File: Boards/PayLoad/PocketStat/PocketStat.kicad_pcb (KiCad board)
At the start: 4 copper layers, 46 x 46 mm, 71 parts, among them J20 DX07S016JA1R1500, J3 MEM2061-01-188-00-A_REVA, J5 BM03B-SRSS-TBLFSN, Q1 BC857CMB_315, U1 HDC2080DMBR, U4 LPS22DFTR, U5 W25Q128JVSIQ TR, U6 BMP581, U8 ST1L05APU33R

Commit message: PocketStat update
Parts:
- removed R1, R2: 2k, Resistor-0402:RES_0402
- added R26: 2k, Resistor-0402:RES_0402, F.Cu at (126.6, 96.9)
- added R27: 2k, Resistor-0402:RES_0402, F.Cu at (124.1, 98.3)
- moved C1 12.6 mm to (121.2, 96.1), turned to -90 degrees
- moved C5 11.6 mm to (132.3, 98.5), turned to 0 degrees
- moved C13 11.6 mm to (130.9, 78.2), turned to 180 degrees
- moved C3 10.3 mm to (130.9, 79.5), turned to 0 degrees
- moved C2 9.09 mm to (122.5, 96.1), turned to -90 degrees
- moved CR1 9.05 mm to (141.2, 79.7), turned to 0 degrees
- moved U6 8.37 mm to (130.9, 81.6), turned to 0 degrees
- moved HM1 8.37 mm to (132.3, 96.3)
- moved C4 8.29 mm to (130.1, 96.4)
- moved U4 7.52 mm to (124.5, 96.3), turned to 90 degrees
- moved Q1 6.59 mm to (135.3, 78.9), turned to 90 degrees
- moved R20 6.29 mm to (137.2, 79.2), turned to 180 degrees
- moved C24 5.75 mm to (141.0, 75.2), turned to -90 degrees
- moved R21 4.68 mm to (137.2, 80.4), turned to 180 degrees
- moved C22 3.75 mm to (139.8, 75.2), turned to -90 degrees
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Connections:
- HM1 pad 2: +3.3V -> /HUM ~{CS} SPI
- HM1 pad 3: /SDA1 I2C -> /MOSI1 SPI
- HM1 pad 4: /SCL1 I2C -> /SCK1 SPI
- HM1 pad 5: GND -> /MISO1 SPI
- MCU2 pad 12: /BAR1 ~{CS} SPI -> /HUM ~{CS} SPI
- MCU2 pad 15: /BAR2 RDY -> unconnected-(MCU2-GPIO12-Pad15)
- MCU2 pad 16: /BAR2 ~{CS} SPI -> unconnected-(MCU2-GPIO13-Pad16)
- MCU2 pad 18: unconnected-(MCU2-GPIO15-Pad18) -> /LED Status
- MCU2 pad 2: unconnected-(MCU2-GPIO0-Pad2) -> /BAR1 RDY
- MCU2 pad 31: /LED Status -> unconnected-(MCU2-GPIO20-Pad31)
- MCU2 pad 32: unconnected-(MCU2-GPIO21-Pad32) -> /BAR2 RDY
- MCU2 pad 35: /Humidity RDY -> unconnected-(MCU2-GPIO23-Pad35)
- MCU2 pad 38: unconnected-(MCU2-GPIO26_ADC0-Pad38) -> /Humidity RDY
- MCU2 pad 6: /BAR1 RDY -> unconnected-(MCU2-GPIO4-Pad6)
- U4 pad 2: /SCK1 SPI -> /SCL1 I2C
- U4 pad 4: /MOSI1 SPI -> /SDA1 I2C
- U4 pad 5: /MISO1 SPI -> GND
- U4 pad 6: /BAR1 ~{CS} SPI -> +3.3V
- U6 pad 2: /SCK1 SPI -> /SCL0 I2C
- U6 pad 4: /MOSI1 SPI -> /SDA0 I2C
- U6 pad 5: /MISO1 SPI -> GND
- U6 pad 6: /BAR2 ~{CS} SPI -> unconnected-(U6-CSB-Pad6)
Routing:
- net /LED Status: track 3.05 -> 16.2 mm, vias 0 -> 2
- net /BAR1 ~{CS} SPI: track 6.76 -> 0.00 mm, vias 2 -> 0
- net /SCK1 SPI: track 6.46 -> 0.00 mm, vias 2 -> 0
- net /SCL1 I2C: track 4.58 -> 9.56 mm, vias 0 -> 2
- net +6V: track 0.00 -> 4.17 mm, vias 0 -> 1
- net /Crystal: track 0.00 -> 4.13 mm
- net GND: track 5.94 -> 9.88 mm
- net +3.3V: track 29.2 -> 33.0 mm
- net VBUS: track 11.5 -> 15.2 mm
- net /Humidity RDY: track 0.00 -> 3.49 mm, vias 0 -> 1
- net /MISO1 SPI: track 2.92 -> 0.00 mm
- net /HUM ~{CS} SPI: track 0.00 -> 2.69 mm
- net /MOSI1 SPI: track 2.63 -> 0.00 mm
- net /BAR1 RDY: track 6.12 -> 3.50 mm
- net /D+: track 14.3 -> 13.7 mm
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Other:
- board size 46 x 46 mm -> 45.5 x 45.5 mm

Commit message: Pocket Stat Lib update
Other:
- board text added: "TODO: 1- Fazer BOOM e atualizar excel de componentes 2- Routing crítico (Sinais Digitais) -> Fazer DRC no fim 3- Routing +3.3V -> Fazer DRC no fim 4- Routing +6V -> Fazer DRC no fim 5- Routing GND (Fazer ground planes) -> Fazer DRC no fim 6- Adicionar Test Points (GND, +3V3, +6V) 7- Fazer Silkscreen Bonito (Vai se ter de editar o Silkcreen de algumas footprints) (+ Assinar e Logo da PST) 8- Prepa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"
- board text removed: "TODO: 1- Routing crítico (Sinais Digitais) -> Fazer DRC no fim 2- Routing +3.3V -> Fazer DRC no fim 3- Routing +6V -> Fazer DRC no fim 4- Routing GND (Fazer ground planes) -> Fazer DRC no fim 5- Adicionar Test Points (GND, +3V3, +6V) 7- Fazer Silkscreen Bonito (Vai se ter de editar o Silkcreen de algumas footprints) (+ Assinar e Logo da PST) 8- Fazer BOOM e atualizar excel de componentes 9- Prepa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"
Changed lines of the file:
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@@
 			)
 		)
-		(fp_text user "${REFERENCE}"
-			(at 0 0 90)
+		(fp_text user "*"
+			(at -2.3114 -2.6162 90)
 			(unlocked yes)
 			(layer "F.Fab")
@@
 			)
 		)
-		(fp_text user "*"
-			(at -2.3114 -2.6162 90)
+		(fp_text user "${REFERENCE}"
+			(at 0 0 90)
 			(unlocked yes)
 			(layer "F.Fab")
@@
 		(layer "User.4")
 	)
-	(gr_text "TODO:\n1- Routing crítico (Sinais Digitais) -> Fazer DRC no fim\n2- Routing +3.3V -> Fazer DRC no fim\n3- Routing +6V  -> Fazer DRC no fim\n4- Routing GND (Fazer ground planes) -> Fazer DRC no fim\n5- Adicionar Test Points (GND, +3V3, +6V)\n7- Fazer Silkscreen Bonito\n(Vai se ter de editar o Silkcreen de algumas footprints)\n(+ Assinar e Logo da PST)\n8- Fazer BOOM e atualizar excel de componentes\n9- Preparar ficheiros de fabrico -> Tapeout\n---\nO Stackup é:\nTop Layer: Signal/PWR\nInner Layer 1: GND\nInner Layer 2: GND\nBottom Layer: Signal/PWR"
+	(gr_text "TODO:\n1- Fazer BOOM e atualizar excel de componentes\n2- Routing crítico (Sinais Digitais) -> Fazer DRC no fim\n3- Routing +3.3V -> Fazer DRC no fim\n4- Routing +6V  -> Fazer DRC no fim\n5- Routing GND (Fazer ground planes) -> Fazer DRC no fim\n6- Adicionar Test Points (GND, +3V3, +6V)\n7- Fazer Silkscreen Bonito\n(Vai se ter de editar o Silkcreen de algumas footprints)\n(+ Assinar e Logo da PST)\n8- Preparar ficheiros de fabrico -> Tapeout\n---\nO Stackup é:\nTop Layer: Signal/PWR\nInner Layer 1: GND\nInner Layer 2: GND\nBottom Layer: Signal/PWR"
 		(at 99.4 142.45 0)
 		(layer "User.1")
@@
 		(net 6)
 	)
-	(segment
-		(start 113.221499 94.796501)
-		(end 113.3 94.875002)
-		(width 0.5)
-		(layer "F.Cu")
-		(net 6)
-	)
 	(via
 		(at 114.349999 91.9)
@@
 	)
 	(segment
-		(start 125.2 81.05)
-		(end 125.9 81.75)
+		(start 125.9 81.75)
+		(end 127.2 81.75)
 		(width 0.125)
 		(layer "B.Cu")
@@
 	)
 	(segment
-		(start 125.9 81.75)
-		(end 127.2 81.75)
+		(start 125.2 81.05)
+		(end 125.9 81.75)
 		(width 0.125)
 		(layer "B.Cu")
@@
 	)
 	(segment
-		(start 126.381009 92.578145)
+		(start 126.381009 92.573519)
 		(end 126.381009 92.56231)
 		(width 0.125)
@@
 	)
 	(segment
-		(start 118.685 92.615)
-		(end 119.2 92.1)
-		(width 0.25)
+		(start 126.377296 92.577232)
+		(end 126.381009 92.573519)
+		(width 0.125)
 		(layer "F.Cu")
 		(net 52)
 	)
 	(segment
-		(start 126.381009 92.56231)
-		(end 125.918698 92.099999)
-		(width 0.125)
+		(start 118.685 92.615)
+		(end 119.2 92.1)
+		(width 0.25)
 		(layer "F.Cu")
 		(net 52)
@@
 		(net 52)
 	)
+	(segment
+		(start 126.381009 92.56231)
+		(end 125.918698 92.099999)
+		(width 0.125)
+		(layer "F.Cu")
+		(net 52)
+	)
 	(via
 		(at 119.2 92.1)
@@
 	)
 	(via
-		(at 126.381009 92.578145)
+		(at 126.377296 92.577232)
 		(size 0.5)
 		(drill 0.2)
@@
 	)
 	(segment
-		(start 126.4 91.7)
-		(end 125.2964 91.7)
+		(start 126.546312 91.846312)
+		(end 126.4 91.7)
 		(width 0.125)
 		(layer "F.Cu")
@@
 	)
 	(segment
-		(start 126.546312 91.846312)
-		(end 126.4 91.7)
+		(start 126.4 91.7)
+		(end 125.2964 91.7)
 		(width 0.125)
 		(layer "F.Cu")
@@
 	)
 	(segment
-		(start 126.348372 91.7)
-		(end 120.2 91.7)
+		(start 126.546312 91.89794)
+		(end 126.348372 91.7)
 		(width 0.125)
 		(layer "B.Cu")
@@
 	)
 	(segment
-		(start 126.546312 91.89794)
-		(end 126.348372 91.7)
+		(start 126.348372 91.7)
+		(end 120.2 91.7)
 		(width 0.125)
 		(layer "B.Cu")

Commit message: pocketstat power update
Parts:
- D1, D2: value RSX301L-30DDTE25 -> PMEG2010ER; footprint Diode-Schottky_RSX301L:DIOM5026X220N -> Diode-Schottky_PMEG2010ER:SODFL3517X110N
- moved C27 1.62 mm to (122.6, 57.3)
- moved C6 1.62 mm to (122.6, 56.1)
- moved D1 1.35 mm to (111.6, 93.6)
- moved JP4 1.35 mm to (112.4, 96.7)
- moved R22 0.96 mm to (115.3, 96.6), turned to 0 degrees
- moved D2 0.55 mm to (118.6, 56.6)
- moved JP6 0.46 mm to (113.6, 56.8)
- moved BT1 0.46 mm to (112.6, 71.5)
- moved R10 0.26 mm to (113.7, 90.3)
- moved C36 0.26 mm to (112.6, 91.6)
- moved D4 0.26 mm to (110.7, 89.7)
- moved J20 0.26 mm to (105.7, 90.2)
- moved R11 0.26 mm to (113.7, 89.1)
- moved R24 0.26 mm to (109.2, 91.6)
- moved R9 0.26 mm to (108.5, 87.6)
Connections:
- C22 pad 2: +6V -> +5V
- C24 pad 2: +6V -> +5V
- C27 pad 1: +6V -> +5V
- C36 pad 1: +6V -> +5V
- C6 pad 1: +6V -> +5V
- CR1 pad 2: +6V -> +5V
- JP6 pad 1: Net-(D2-A) -> Net-(JP6-A)
- U8 pad 3: +6V -> +5V
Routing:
- net +5V: track 0.00 -> 5.93 mm, vias 0 -> 1
- net +6V: track 4.06 -> 0.00 mm, vias 1 -> 0
- net Net-(JP6-A): track 0.00 -> 2.88 mm
- net Net-(D2-A): track 2.52 -> 0.00 mm
- removed copper zone on F.Cu, net +6V

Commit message: update
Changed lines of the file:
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@@
 		)
 		(fp_text user "*"
-			(at -1.535 -0.881 0)
+			(at -0.959999 -0.631 0)
 			(unlocked yes)
 			(layer "F.SilkS")
@@
 		)
 		(fp_text user "*"
-			(at -1.535 -0.881 0)
+			(at -0.969999 -0.633001 0)
 			(unlocked yes)
 			(layer "F.SilkS")

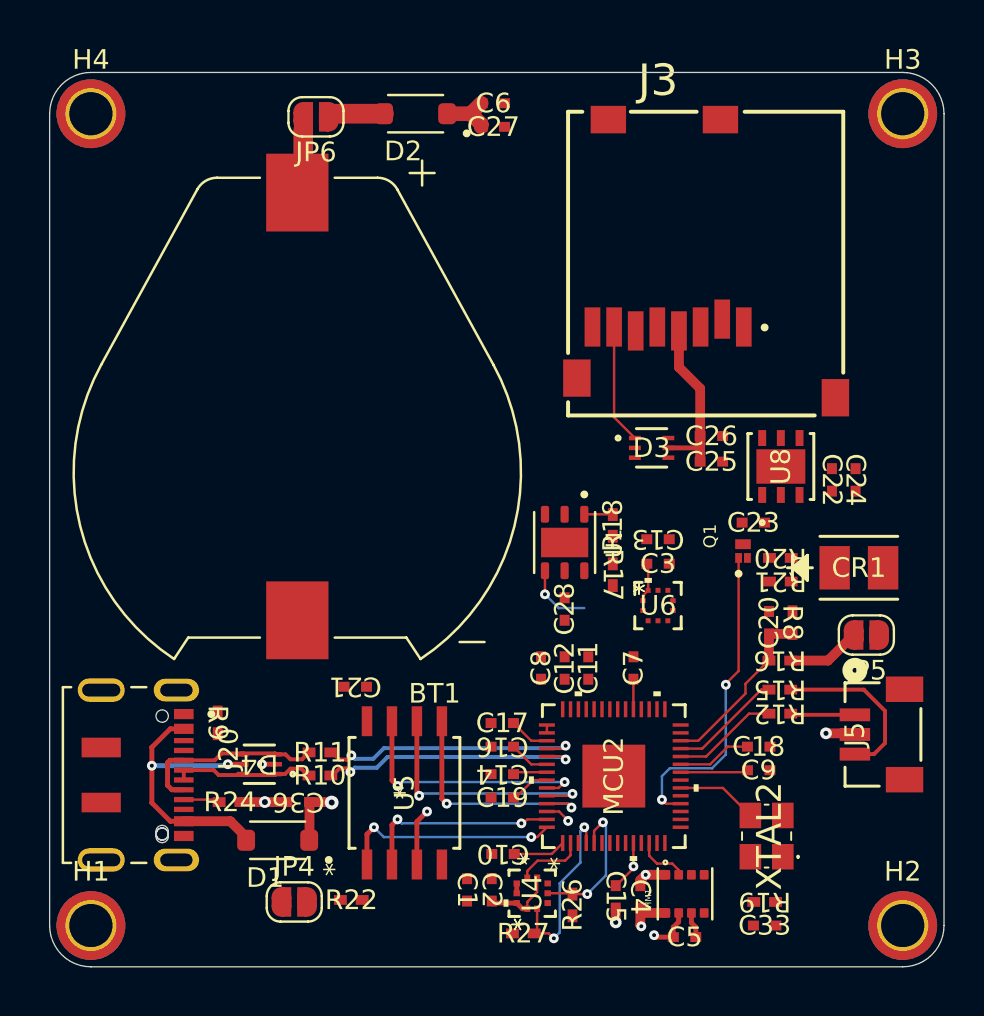
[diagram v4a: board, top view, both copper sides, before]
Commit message: Update PCB Payload
Acabei o routing do ground e coloquei as camadas de GND;
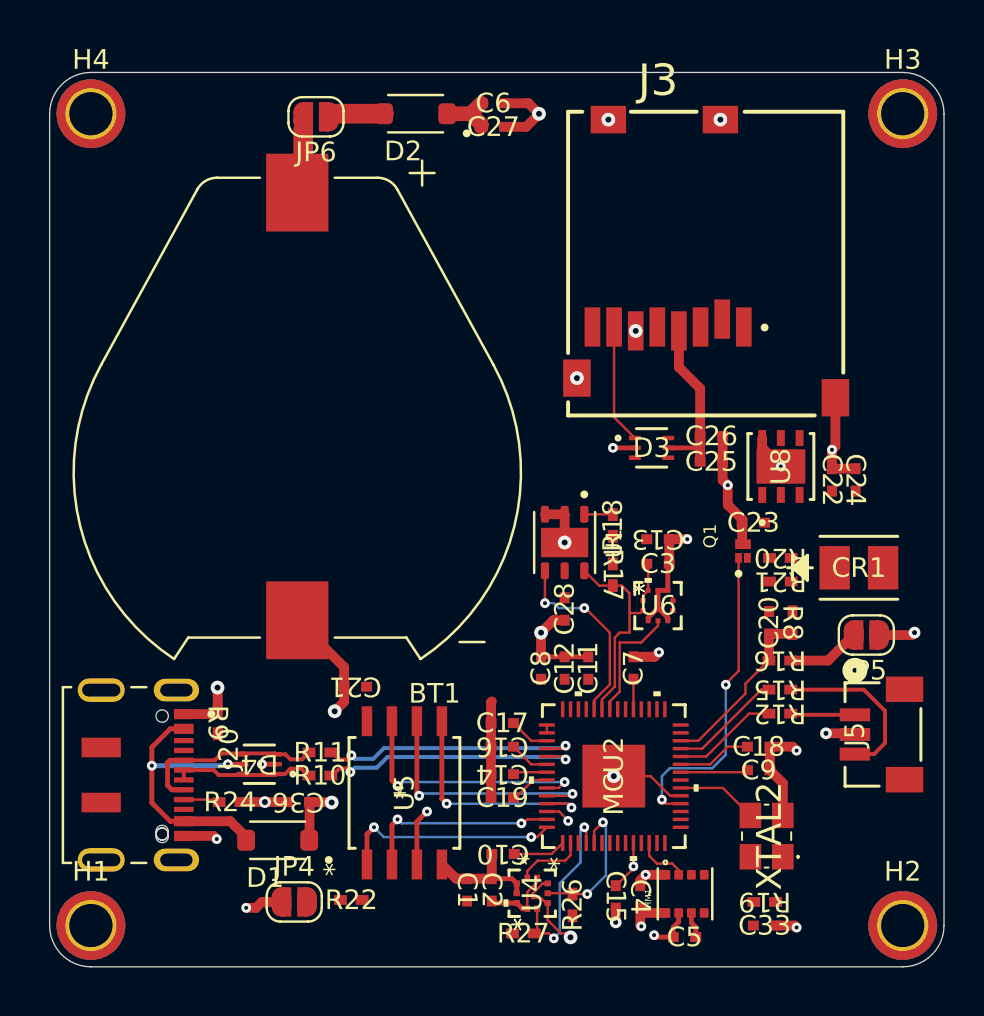
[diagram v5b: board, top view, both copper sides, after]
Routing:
- net GND: track 9.88 -> 82.6 mm, vias 6 -> 28
- net /SCL0 I2C: track 0.00 -> 10.3 mm
- net /Humidity RDY: track 3.49 -> 9.80 mm, vias 1 -> 2
- net /SDA0 I2C: track 1.46 -> 7.61 mm
- added copper zone on In1.Cu, net GND
- added copper zone on In2.Cu, net GND
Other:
- board text added: "X"

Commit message: Update PocketStat.kicad_pcb
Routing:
- net +3.3V: track 33.0 -> 91.4 mm, vias 2 -> 7
- net +5V: track 5.93 -> 48.1 mm
- net /BAR2 RDY: track 0.00 -> 9.80 mm
- net /MISO1 SPI: track 0.00 -> 5.41 mm, vias 0 -> 2
- net /MOSI1 SPI: track 0.17 -> 5.27 mm
- net /SCK1 SPI: track 0.00 -> 3.62 mm
- net /SDA1 I2C: track 7.43 -> 4.33 mm, vias 2 -> 0
- net Net-(XTAL2-TRI-STATE(STBY)): track 0.00 -> 2.45 mm
- net /MCU ~{CS} SPI: track 11.3 -> 13.2 mm
- net /USB ~{BOOT}: track 0.00 -> 1.74 mm
- net GND: track 82.6 -> 82.0 mm, vias 28 -> 29

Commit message: minor changes
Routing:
- net GND: track 82.0 -> 76.5 mm, vias 29 -> 38
- net +5V: track 48.1 -> 43.9 mm
- net +3.3V: track 91.4 -> 92.9 mm

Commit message: minor changes
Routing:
- net +3.3V: track 92.9 -> 96.4 mm
- net +5V: track 43.9 -> 46.0 mm
- net GND: track 76.5 -> 78.4 mm, vias 38 -> 61
